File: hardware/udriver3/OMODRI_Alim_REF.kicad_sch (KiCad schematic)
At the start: 5 parts, among them U5 LT6654AIS6-3

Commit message: Schematics update. 12V0 and 5V0 power supplies not finished yet. RS485 added but not connected to F28388 mcu.
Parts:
- C26: Rated Voltage 10V -> 25V
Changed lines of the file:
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@@
     (title "Open MOtor DRiver Initiative (OMODRI)")
     (date "2020-12-16")
-    (rev "1.1")
+    (rev "2.0")
     (company "LAAS/CNRS")
   )
@@
       (effects (font (size 1.27 1.27)) hide)
     )
-    (property "Rated Voltage" "10V" (id 9) (at 142.24 93.98 0)
+    (property "Rated Voltage" "25V" (id 9) (at 142.24 93.98 0)
       (effects (font (size 1.27 1.27)) hide)
     )

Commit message: Temporary version of udrive3 v2.0. - In schematic there are 2 solutions for DC/DC buck converter. - PCB routing is not finished yet.
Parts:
- C28: footprint Capacitor_SMD:C_0603_1608Metric -> Capacitor_SMD:C_0402_1005Metric; DigiKey 490-10475-1-ND -> 490-13238-2-ND; Farnell 2456110 -> 3582794; Mouser 81-GRM188R61A106ME9D -> 81-GRM155R60J106ME5D; Part No GRM188R61A106ME69D -> GRM155R60J106ME15D; RS 113-8702 -> (none); Rated Voltage 10V -> 6.3V
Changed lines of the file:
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@@
   (title_block
     (title "Open MOtor DRiver Initiative (OMODRI)")
-    (date "2020-12-16")
+    (date "2022-10-05")
     (rev "2.0")
     (company "LAAS/CNRS")
@@
   (wire (pts (xy 142.24 80.645) (xy 146.05 80.645))
     (stroke (width 0) (type default) (color 0 0 0 0))
-  )
-  (label "REF_3V0" (at 169.545 80.645 0)
-    (effects (font (size 1.27 1.27)) (justify left bottom))
   )
   (global_label "REF_3V0_BUF" (shape output) (at 180.975 80.645 0) (fields_autoplaced)
@@
       (effects (font (size 1.27 1.27)) (justify left))
     )
-    (property "Footprint" "Capacitor_SMD:C_0603_1608Metric" (id 2) (at 168.6052 99.06 0)
+    (property "Footprint" "Capacitor_SMD:C_0402_1005Metric" (id 2) (at 168.6052 99.06 0)
       (effects (font (size 1.27 1.27)) hide)
     )
@@
       (effects (font (size 1.27 1.27)) hide)
     )
-    (property "DigiKey" "490-10475-1-ND" (id 4) (at 167.64 95.25 0)
-      (effects (font (size 1.27 1.27)) hide)
-    )
-    (property "Farnell" "2456110" (id 5) (at 167.64 95.25 0)
-      (effects (font (size 1.27 1.27)) hide)
-    )
-    (property "Mouser" "81-GRM188R61A106ME9D" (id 6) (at 167.64 95.25 0)
-      (effects (font (size 1.27 1.27)) hide)
-    )
-    (property "Part No" "GRM188R61A106ME69D" (id 7) (at 167.64 95.25 0)
-      (effects (font (size 1.27 1.27)) hide)
-    )
-    (property "RS" "113-8702" (id 8) (at 167.64 95.25 0)
-      (effects (font (size 1.27 1.27)) hide)
-    )
-    (property "Rated Voltage" "10V" (id 9) (at 167.64 95.25 0)
-      (effects (font (size 1.27 1.27)) hide)
-    )
+    (property "DigiKey" "490-13238-2-ND" (id 4) (at 167.64 95.25 0)
+      (effects (font (size 1.27 1.27)) hide)
+    )
+    (property "Farnell" "3582794" (id 5) (at 167.64 95.25 0)
+      (effects (font (size 1.27 1.27)) hide)
+    )
+    (property "Mouser" "81-GRM155R60J106ME5D" (id 6) (at 167.64 95.25 0)
+      (effects (font (size 1.27 1.27)) hide)
+    )
+    (property "Part No" "GRM155R60J106ME15D" (id 7) (at 167.64 95.25 0)
+      (effects (font (size 1.27 1.27)) hide)
+    )
+    (property "RS" "" (id 8) (at 167.64 95.25 0)
+      (effects (font (size 1.27 1.27)) hide)
+    )
+    (property "Rated Voltage" "6.3V" (id 9) (at 167.64 95.25 0)
+      (effects (font (size 1.27 1.27)) hide)
+    )

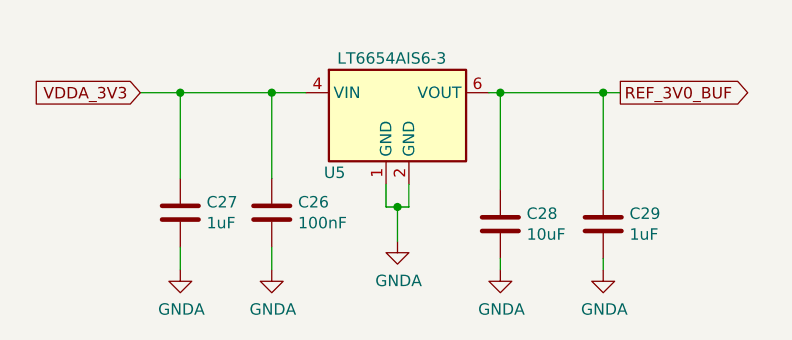
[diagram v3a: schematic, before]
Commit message: PCB update. Re-annotation of the design + via stitching (GND).
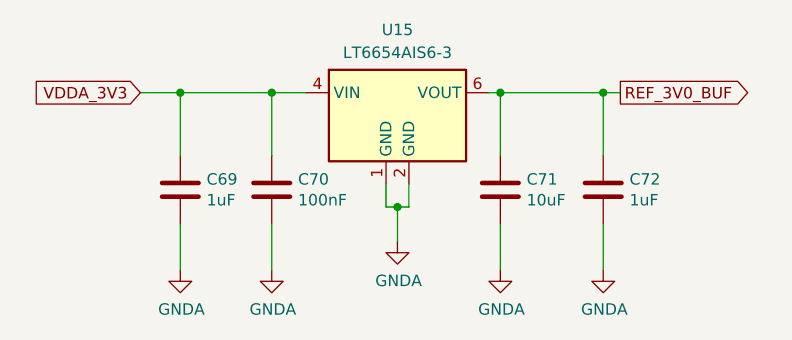
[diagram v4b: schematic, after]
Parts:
- renumbered C27 to C69, C26 to C70, C28 to C71, C29 to C72, U5 to U15
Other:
- moved on the sheet: C69, C70, C71, C72

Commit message: PCB updates - FSI protection added against FPC cable reverse connection - BOSCH BMI088 IMU added.
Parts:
- renumbered C69 to C70, C70 to C71, C71 to C72, C72 to C73
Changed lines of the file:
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@@
   (title_block
     (title "Open MOtor DRiver Initiative (OMODRI)")
-    (date "2022-10-05")
+    (date "2022-11-24")
     (rev "2.0")
     (company "LAAS/CNRS")
@@
   (symbol (lib_id "power:GNDA") (at 132.08 100.33 0) (unit 1)
     (in_bom yes) (on_board yes)
-    (property "Reference" "#PWR0144" (id 0) (at 132.08 106.68 0)
+    (property "Reference" "#PWR0145" (id 0) (at 132.08 106.68 0)
       (effects (font (size 1.27 1.27)) hide)
     )
@@
   (symbol (lib_id "power:GNDA") (at 142.24 100.33 0) (unit 1)
     (in_bom yes) (on_board yes)
-    (property "Reference" "#PWR0145" (id 0) (at 142.24 106.68 0)
+    (property "Reference" "#PWR0146" (id 0) (at 142.24 106.68 0)
       (effects (font (size 1.27 1.27)) hide)
     )
@@
   (symbol (lib_id "power:GNDA") (at 156.21 97.155 0) (unit 1)
     (in_bom yes) (on_board yes)
-    (property "Reference" "#PWR0143" (id 0) (at 156.21 103.505 0)
+    (property "Reference" "#PWR0144" (id 0) (at 156.21 103.505 0)
       (effects (font (size 1.27 1.27)) hide)
     )
@@
   (symbol (lib_id "Device:C") (at 142.24 91.44 0) (unit 1)
     (in_bom yes) (on_board yes)
-    (property "Reference" "C70" (id 0) (at 145.161 90.2716 0)
+    (property "Reference" "C71" (id 0) (at 145.161 90.2716 0)
       (effects (font (size 1.27 1.27)) (justify left))
     )
@@
   (symbol (lib_id "Device:C") (at 132.08 91.44 0) (unit 1)
     (in_bom yes) (on_board yes)
-    (property "Reference" "C69" (id 0) (at 135.001 90.2716 0)
+    (property "Reference" "C70" (id 0) (at 135.001 90.2716 0)
       (effects (font (size 1.27 1.27)) (justify left))
     )
@@
   (symbol (lib_id "Device:C") (at 167.64 91.44 0) (unit 1)
     (in_bom yes) (on_board yes)
-    (property "Reference" "C71" (id 0) (at 170.561 90.2716 0)
+    (property "Reference" "C72" (id 0) (at 170.561 90.2716 0)
       (effects (font (size 1.27 1.27)) (justify left))
     )
@@
   (symbol (lib_id "Device:C") (at 179.07 91.44 0) (unit 1)
     (in_bom yes) (on_board yes)
-    (property "Reference" "C72" (id 0) (at 181.991 90.2716 0)
+    (property "Reference" "C73" (id 0) (at 181.991 90.2716 0)
       (effects (font (size 1.27 1.27)) (justify left))
     )
@@
   (symbol (lib_id "power:GNDA") (at 167.64 100.33 0) (unit 1)
     (in_bom yes) (on_board yes)
-    (property "Reference" "#PWR0146" (id 0) (at 167.64 106.68 0)
+    (property "Reference" "#PWR0147" (id 0) (at 167.64 106.68 0)
       (effects (font (size 1.27 1.27)) hide)
     )
@@
   (symbol (lib_id "power:GNDA") (at 179.07 100.33 0) (unit 1)
     (in_bom yes) (on_board yes)
-    (property "Reference" "#PWR0147" (id 0) (at 179.07 106.68 0)
-      (effects (font (size 1.27 1.27)) hide)
-    )
+    (property "Reference" "#PWR0148" (id 0) (at 179.07 106.68 0)
+      (effects (font (size 1.27 1.27)) hide)
+    )

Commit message: PCB udpates. - add serial resistors on boot jumpers - modify config jumpers to be opened by default
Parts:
- renumbered C70 to C68, C71 to C69, C72 to C70, C73 to C71, U15 to U14
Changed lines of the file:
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@@
   (symbol (lib_id "omodri_lib:LT6654AIS6-3") (at 156.21 83.185 0) (unit 1)
     (in_bom yes) (on_board yes)
-    (property "Reference" "U15" (id 0) (at 156.21 73.66 0))
+    (property "Reference" "U14" (id 0) (at 156.21 73.66 0))
     (property "Value" "LT6654AIS6-3" (id 1) (at 156.21 76.2 0))
     (property "Footprint" "Package_TO_SOT_SMD:TSOT-23-6" (id 2) (at 158.75 74.295 0)
@@
   (symbol (lib_id "power:GNDA") (at 132.08 100.33 0) (unit 1)
     (in_bom yes) (on_board yes)
-    (property "Reference" "#PWR0145" (id 0) (at 132.08 106.68 0)
+    (property "Reference" "#PWR0131" (id 0) (at 132.08 106.68 0)
       (effects (font (size 1.27 1.27)) hide)
     )
@@
   (symbol (lib_id "power:GNDA") (at 142.24 100.33 0) (unit 1)
     (in_bom yes) (on_board yes)
-    (property "Reference" "#PWR0146" (id 0) (at 142.24 106.68 0)
+    (property "Reference" "#PWR0132" (id 0) (at 142.24 106.68 0)
       (effects (font (size 1.27 1.27)) hide)
     )
@@
   (symbol (lib_id "power:GNDA") (at 156.21 97.155 0) (unit 1)
     (in_bom yes) (on_board yes)
-    (property "Reference" "#PWR0144" (id 0) (at 156.21 103.505 0)
+    (property "Reference" "#PWR0130" (id 0) (at 156.21 103.505 0)
       (effects (font (size 1.27 1.27)) hide)
     )
@@
   (symbol (lib_id "Device:C") (at 142.24 91.44 0) (unit 1)
     (in_bom yes) (on_board yes)
-    (property "Reference" "C71" (id 0) (at 145.161 90.2716 0)
+    (property "Reference" "C69" (id 0) (at 145.161 90.2716 0)
       (effects (font (size 1.27 1.27)) (justify left))
     )
@@
   (symbol (lib_id "Device:C") (at 132.08 91.44 0) (unit 1)
     (in_bom yes) (on_board yes)
-    (property "Reference" "C70" (id 0) (at 135.001 90.2716 0)
+    (property "Reference" "C68" (id 0) (at 135.001 90.2716 0)
       (effects (font (size 1.27 1.27)) (justify left))
     )
@@
   (symbol (lib_id "Device:C") (at 167.64 91.44 0) (unit 1)
     (in_bom yes) (on_board yes)
-    (property "Reference" "C72" (id 0) (at 170.561 90.2716 0)
+    (property "Reference" "C70" (id 0) (at 170.561 90.2716 0)
       (effects (font (size 1.27 1.27)) (justify left))
     )
@@
   (symbol (lib_id "Device:C") (at 179.07 91.44 0) (unit 1)
     (in_bom yes) (on_board yes)
-    (property "Reference" "C73" (id 0) (at 181.991 90.2716 0)
+    (property "Reference" "C71" (id 0) (at 181.991 90.2716 0)
       (effects (font (size 1.27 1.27)) (justify left))
     )
@@
   (symbol (lib_id "power:GNDA") (at 167.64 100.33 0) (unit 1)
     (in_bom yes) (on_board yes)
-    (property "Reference" "#PWR0147" (id 0) (at 167.64 106.68 0)
+    (property "Reference" "#PWR0133" (id 0) (at 167.64 106.68 0)
       (effects (font (size 1.27 1.27)) hide)
     )
@@
   (symbol (lib_id "power:GNDA") (at 179.07 100.33 0) (unit 1)
     (in_bom yes) (on_board yes)
-    (property "Reference" "#PWR0148" (id 0) (at 179.07 106.68 0)
-      (effects (font (size 1.27 1.27)) hide)
-    )
+    (property "Reference" "#PWR0134" (id 0) (at 179.07 106.68 0)
+      (effects (font (size 1.27 1.27)) hide)
+    )
